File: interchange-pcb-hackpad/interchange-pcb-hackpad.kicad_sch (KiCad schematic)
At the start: 105 parts, among them J1 MagnetR, J2 MagnetL, J3 TRRS_R, J4 TRRS_L, J5 SSD1306, J6 Conn_01x06, U1 Seeeduino Xiao rp2040, U2 PCA9555PW, U3 PCA9555PW, U4 SN74AHCT125PWR

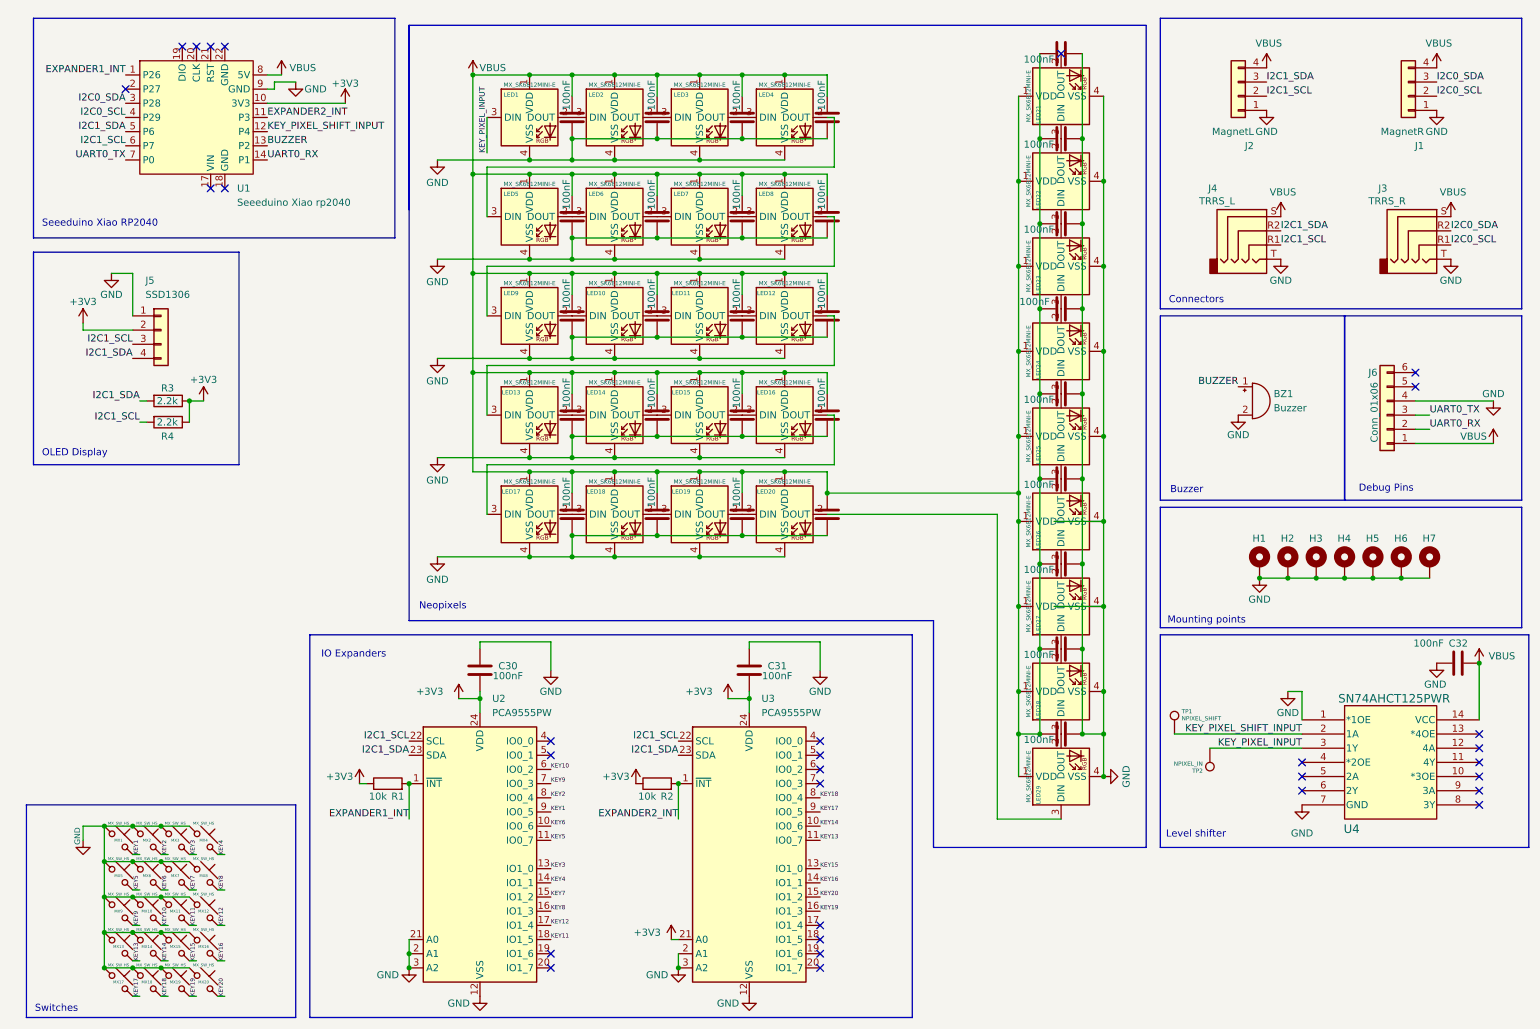
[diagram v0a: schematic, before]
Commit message: feat: create schematic for interchange-pcb-hackpad
and fix minor spacing issues with capaicitors in interchange-pcb-right
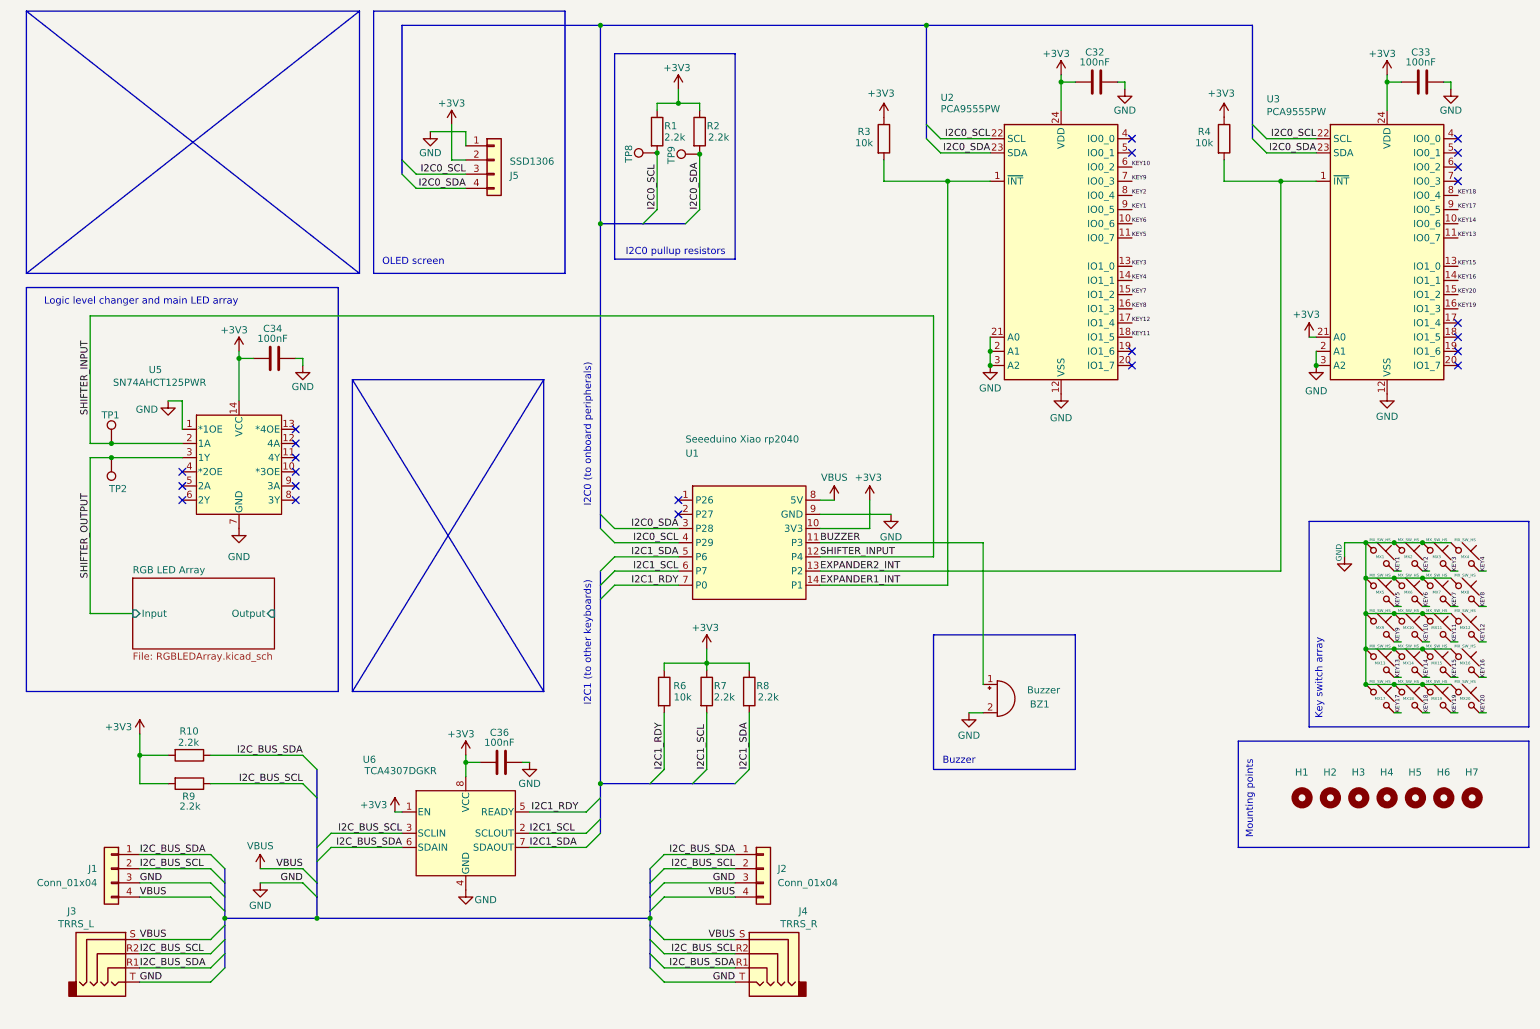
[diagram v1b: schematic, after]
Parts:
- removed C1, C10, C11, C12, C13, C14, C15, C16, C17, C18, C19, C2, C20, C21, C22, C23, C24, C25, C26, C27, C28, C29, C3, C30, C31, C4, C5, C6, C7, C8, C9: 100nF, Capacitor_SMD:C_0603_1608Metric_Pad1.08x0.95mm_HandSolder, symbol Device:C
- removed H1, H2, H3, H4, H5, H6, H7: MountingHole_Pad, MountingHole:MountingHole_3.2mm_M3_Pad_TopBottom, symbol Mechanical:MountingHole_Pad
- removed J6: Conn_01x06, Connector_PinHeader_2.54mm:PinHeader_1x06_P2.54mm_Vertical, symbol Connector_Generic:Conn_01x06
- removed LED1, LED10, LED11, LED12, LED13, LED14, LED15, LED16, LED17, LED18, LED19, LED2, LED20, LED3, LED4, LED5, LED6, LED7, LED8, LED9: MX_SK6812MINI-E, CustomFootprints:LED_MX_6028R-ROT_Custom, symbol PCM_marbastlib-mx:MX_SK6812MINI-E
- removed LED21, LED22, LED23, LED24, LED25, LED26, LED27, LED28, LED29: MX_SK6812MINI-E, CustomFootprints:LED_6028R_Custom, symbol PCM_marbastlib-mx:MX_SK6812MINI-E
- removed U4: SN74AHCT125PWR, CustomFootprints:SN74AHCT125PWR, symbol CustomSymbols:SN74AHCT125PWR
- added C33, C34, C36: 100nF, Capacitor_SMD:C_0603_1608Metric_Pad1.08x0.95mm_HandSolder, symbol Device:C
- added H1, H2, H3, H4, H5, H6, H7: MountingHole_Pad, MountingHole:MountingHole_3.2mm_M3, symbol Mechanical:MountingHole
- added R10, R7, R8, R9: 2.2k, Resistor_SMD:R_0603_1608Metric_Pad0.98x0.95mm_HandSolder, symbol Device:R
- added R6: 10k, Resistor_SMD:R_0603_1608Metric_Pad0.98x0.95mm_HandSolder, symbol Device:R
- added TP8, TP9: TestPoint, TestPoint:TestPoint_Pad_D1.5mm, symbol Connector:TestPoint
- added U5: SN74AHCT125PWR, CustomFootprints:SN74AHCT125PWR, symbol CustomSymbols:SN74AHCT125PWR
- added U6: TCA4307DGKR, CustomFootprints:SOIC8_DGK_TEX, symbol CustomSymbols:TCA4307DGKR
- J1: value MagnetR -> Conn_01x04; footprint CustomFootprints:5358_mag_connector_1x4_pads -> CustomFootprints:MagneticSlot_Right
- J2: value MagnetL -> Conn_01x04; footprint CustomFootprints:5358_mag_connector_1x4_pins -> CustomFootprints:MagneticSlot_Left
- J3: value TRRS_R -> TRRS_L
- J4: value TRRS_L -> TRRS_R
- R1, R2: value 10k -> 2.2k
- R3, R4: value 2.2k -> 10k
- TP1: value NPIXEL_SHIFT -> TestPoint; footprint TestPoint:TestPoint_Pad_1.0x1.0mm -> TestPoint:TestPoint_Pad_D1.5mm
- TP2: value NPIXEL_IN -> TestPoint; footprint TestPoint:TestPoint_Pad_1.0x1.0mm -> TestPoint:TestPoint_Pad_D1.5mm
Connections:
- net UART0_RX is gone; now on net EXPANDER1_INT: U1.14 (P1)
- net +3V3: now also C32.2, C33.2, C34.2, C36.2, R10.2, R6.1, R7.1, R8.1, R9.2, U5.14 (VCC), U6.1 (EN), U6.8 (VCC)
- net BUZZER: now also U1.11 (P3); no longer U1.13 (P2)
- net EXPANDER1_INT: now also R3.2; no longer R1.2, U1.1 (P26)
- net EXPANDER2_INT: now also R4.2, U1.13 (P2); no longer R2.2, U1.11 (P3)
- net GND: now also J1.3 (Pin_3), J2.3 (Pin_3), C33.1, C34.1, C36.1, U5.1 (*1OE), U5.7 (GND), U6.4 (GND); no longer J1.1 (Pin_1), J2.1 (Pin_1)
- net I2C0_SCL: now also J5.3 (Pin_3), R1.2, U2.22 (SCL), U3.22 (SCL), TP8.1; no longer J1.2 (Pin_2), J3.R1
- net I2C0_SDA: now also J5.4 (Pin_4), R2.2, U2.23 (SDA), U3.23 (SDA), TP9.1; no longer J1.3 (Pin_3), J3.R2
- net I2C1_SCL: now also R7.2, U6.2 (SCLOUT); no longer J2.2 (Pin_2), J4.R1, J5.3 (Pin_3), R4.2, U2.22 (SCL), U3.22 (SCL)
- net I2C1_SDA: now also R8.2, U6.7 (SDAOUT); no longer J2.3 (Pin_3), J4.R2, J5.4 (Pin_4), R3.2, U2.23 (SDA), U3.23 (SDA)
- net VBUS: no longer C32.2
- net KEY_PIXEL_INPUT renamed SHIFTER_OUTPUT
- net SHIFTER_OUTPUT: now also U5.3 (1Y)
- net KEY_PIXEL_SHIFT_INPUT renamed SHIFTER_INPUT
- net SHIFTER_INPUT: now also U5.2 (1A)
- net UART0_TX renamed I2C1_RDY
- net I2C1_RDY: now also R6.2, U6.5 (READY)
- new net I2C_BUS_SCL: J1.2 (Pin_2), J2.2 (Pin_2), J3.R2, J4.R2, R9.1, U6.3 (SCLIN)
- new net I2C_BUS_SDA: J1.1 (Pin_1), J2.1 (Pin_1), J3.R1, J4.R1, R10.1, U6.6 (SDAIN)
- no-connect marks 31 -> 23
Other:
- added sheet RGB LED Array (RGBLEDArray.kicad_sch)
- note added: "I2C0 (to onboard peripherals)"
- note added: "I2C0 pullup resistors"
- note added: "I2C1 (to other keyboards)"
- note added: "Key switch array"
- note added: "Logic level changer and main LED array"
- note added: "OLED screen"
- note removed: "Connectors"
- note removed: "Debug Pins"
- note removed: "IO Expanders"
- note removed: "Level shifter"
- note removed: "Neopixels"
- note removed: "OLED Display"
- note removed: "Seeeduino Xiao RP2040"
- note removed: "Switches"
- title: Slab Keyboard - Hackpad Module -> The Interchange Keyboard - Hackpad Module
